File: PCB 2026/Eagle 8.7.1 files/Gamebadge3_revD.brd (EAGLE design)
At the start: 61 x 85.1 mm, 49 parts, among them IC1 AZ1117IH-3.3TRG1, U1 MCP73832T-5ACI/OT, U2 IS31AP4991A-GRLS2-TR

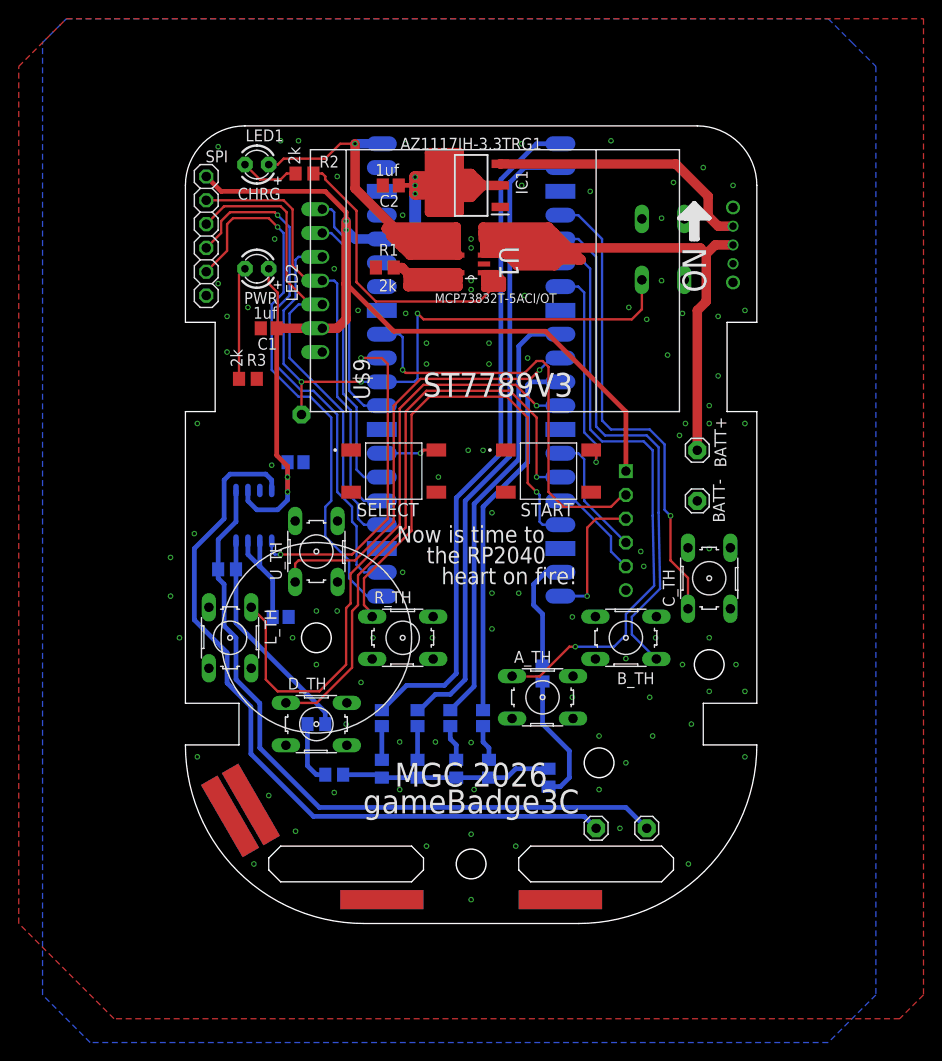
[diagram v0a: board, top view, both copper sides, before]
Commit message: Updated case for 2026 design (ST7789rev3 LCD)
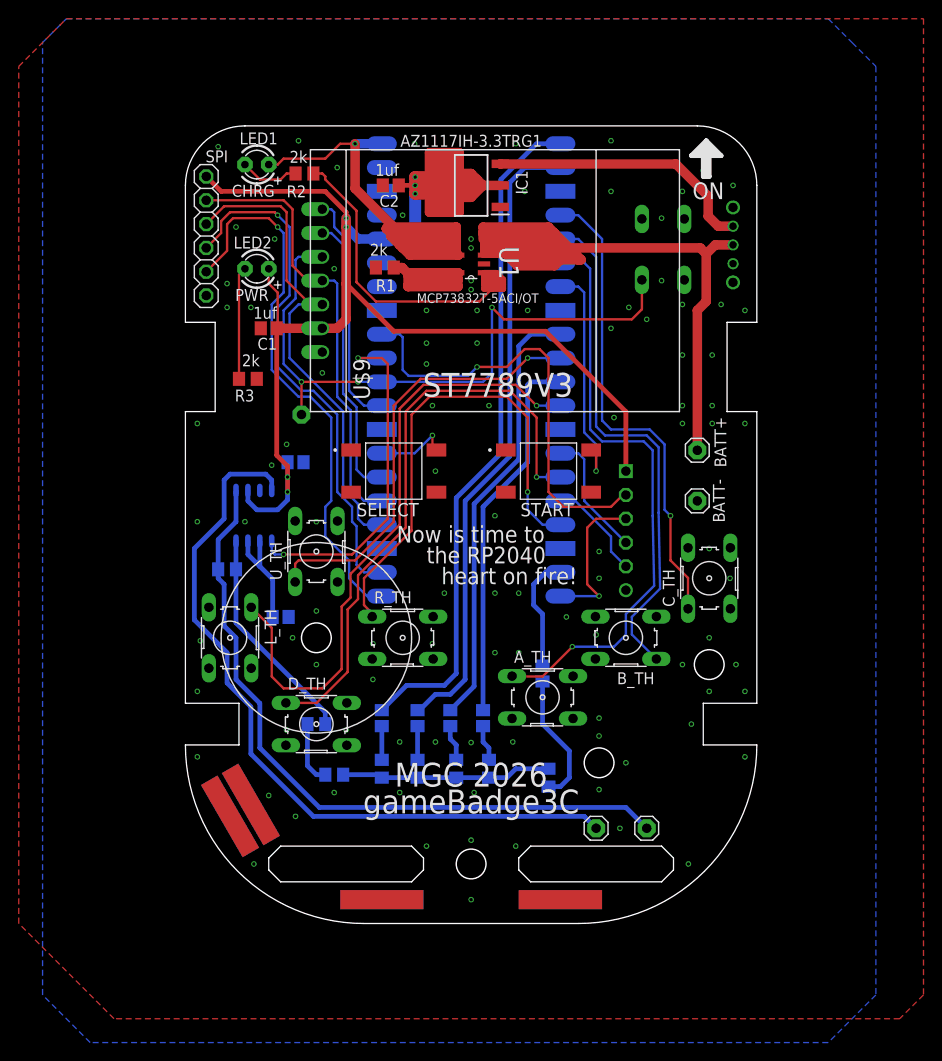
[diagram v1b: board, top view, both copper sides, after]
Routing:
- net SELECT: track 5.96 -> 7.92 mm
- net START: track 23.1 -> 25.0 mm
- net SPI/CS: track 45.1 -> 47.0 mm
- net SPI1_TX: track 14.7 -> 16.5 mm
- net UP: track 46.6 -> 47.5 mm
- net LEFT: track 67.4 -> 66.6 mm
- net AMP_EN: track 37.1 -> 37.7 mm
- net /RST: track 68.1 -> 68.6 mm
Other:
- board text added: "github.com/benheck/gamebadge3"
- board text added: "www.benheck.com"
- board text removed: "350mA"
- board text removed: "M3x3"
- board text removed: "benheck.com"
- board text removed: "github.com/benheck"
